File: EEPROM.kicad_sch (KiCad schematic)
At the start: 22 parts, among them IC1 PCA6408A_TSSOP, IC2 AT24CS01_SOT23, U2 TPS613221A_SOT-23-5

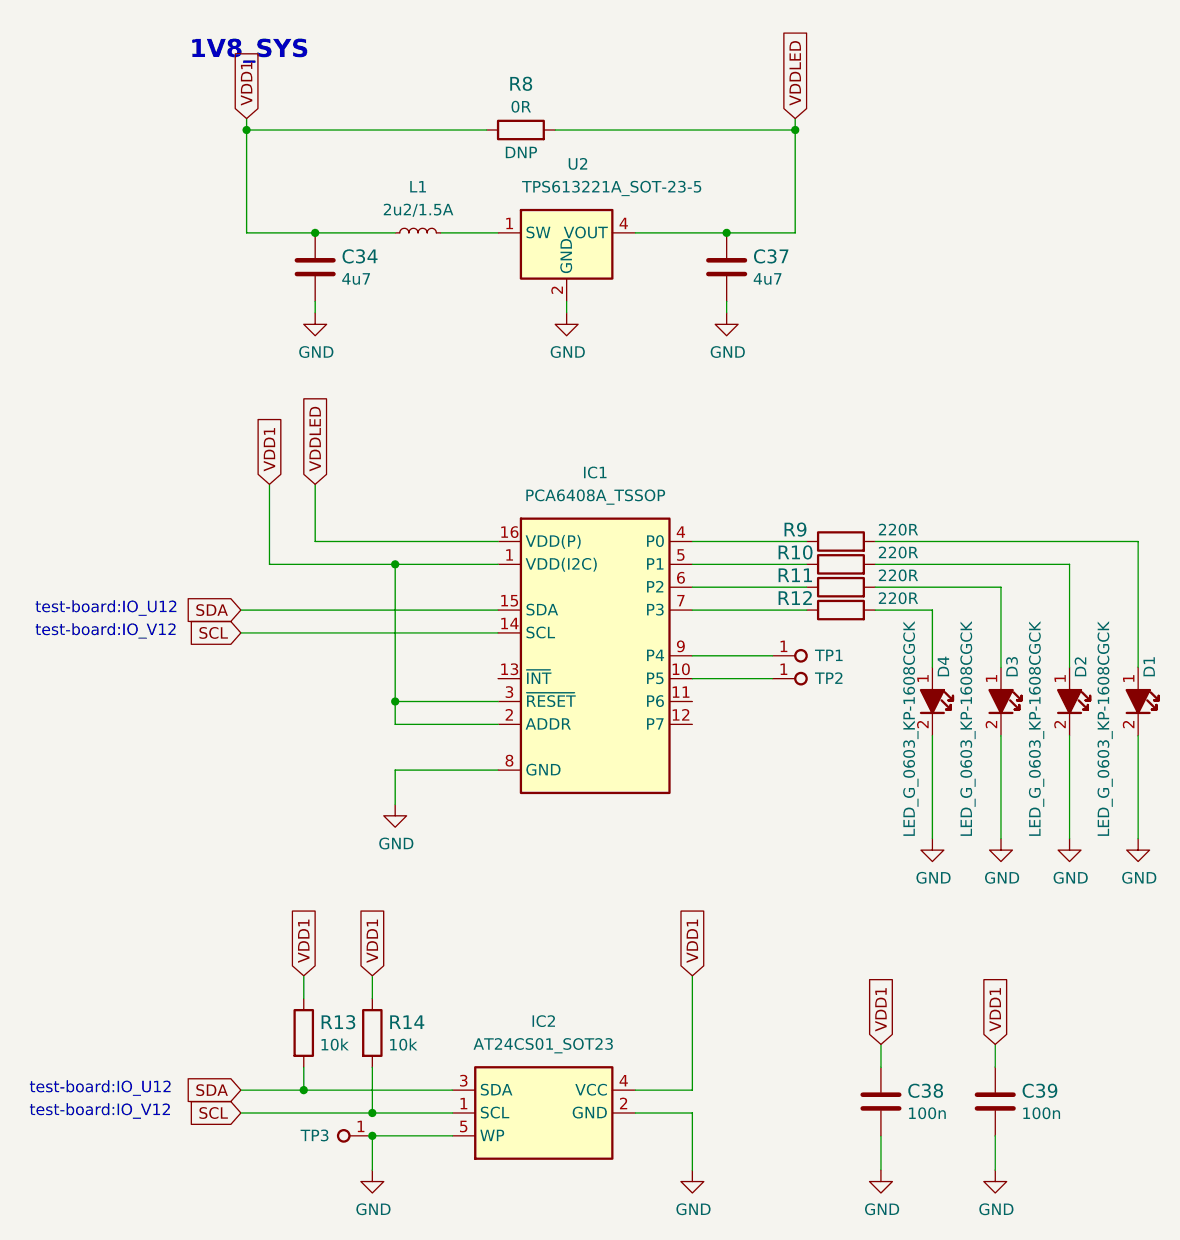
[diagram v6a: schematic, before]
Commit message: Introduce component standardization
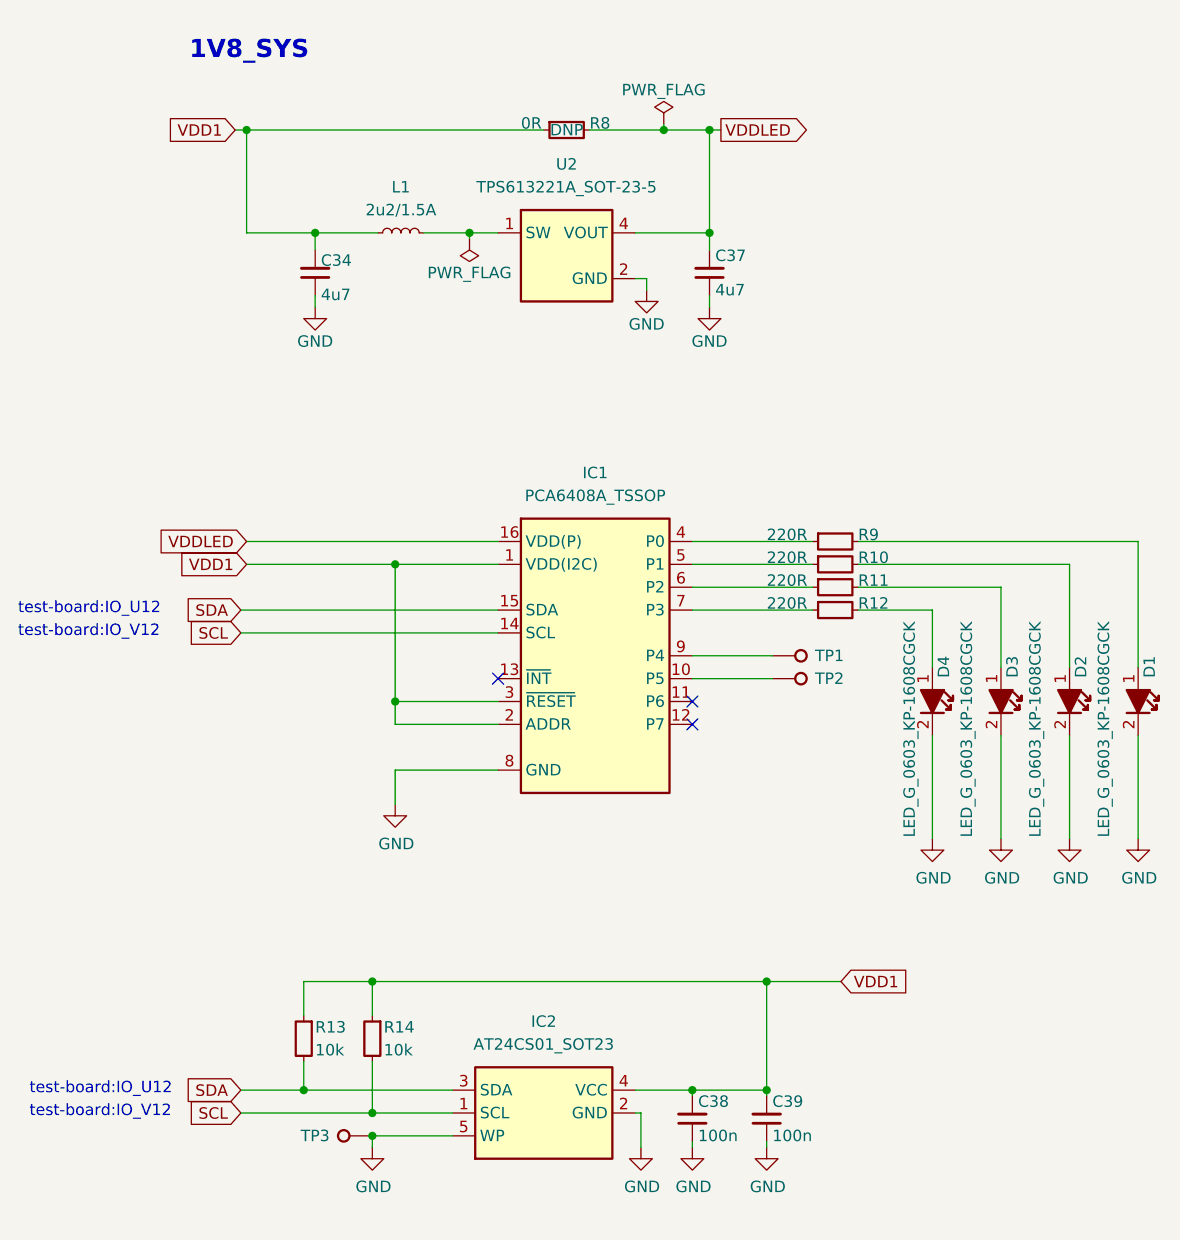
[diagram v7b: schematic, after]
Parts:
- C34, C37: footprint antmicro-footprints:C_0402_1005Metric -> lpddr4-testbed-footprints:C_0402_1005Metric; symbol antmicroCapacitors0402:C_4u7_0402 -> lpddr4-testbed:C_4u7_0402; Author (none) -> Antmicro; License (none) -> Apache-2.0; Manufacturer MURATA -> Murata
- C38, C39: footprint antmicro-footprints:C_0402_1005Metric -> lpddr4-testbed-footprints:C_0402_1005Metric; symbol antmicroCapacitors0402:C_100n_0402 -> lpddr4-testbed:C_100n_0402; Author (none) -> Antmicro; Dielectric (none) -> X5R; License (none) -> Apache-2.0; Voltage (none) -> 50V
- D1, D2, D3, D4: footprint antmicro-footprints:LED_0603_1608Metric_G -> lpddr4-testbed-footprints:LED_0603_1608Metric_G; symbol antmicroLEDIndicationDiscrete:LED_G_0603_KP-1608CGCK -> lpddr4-testbed:LED_G_0603_KP-1608CGCK
- IC1: footprint antmicro-footprints:TSSOP-16_4.4x5mm_P0.65mm -> lpddr4-testbed-footprints:TSSOP-16_4.4x5mm_P0.65mm; symbol antmicroInterfaceIOExpanders:PCA6408A_TSSOP -> lpddr4-testbed:PCA6408A_TSSOP
- IC2: footprint antmicro-footprints:SOT-23-5 -> lpddr4-testbed-footprints:SOT-23-5; symbol antmicroMemory:AT24CS01_SOT23 -> lpddr4-testbed:AT24CS01_SOT23
- L1: footprint antmicro-footprints:L_0806_2016Metric -> lpddr4-testbed-footprints:L_0806_2016Metric; symbol antmicroFixedInductors:L_2u2_1.5A_1285AS-H -> lpddr4-testbed:L_2u2_1.5A_1285AS-H
- R10, R11, R12, R9: footprint antmicro-footprints:R_0402_1005Metric -> lpddr4-testbed-footprints:R_0402_1005Metric; symbol antmicroResistors0402:R_220R_0402 -> lpddr4-testbed:R_220R_0402; Author (none) -> Antmicro; License (none) -> Apache-2.0; Tolerance (none) -> 1%
- R13, R14: footprint antmicro-footprints:R_0402_1005Metric -> lpddr4-testbed-footprints:R_0402_1005Metric; symbol antmicroResistors0402:R_10k_0402 -> lpddr4-testbed:R_10k_0402; Author (none) -> Antmicro; License (none) -> Apache-2.0; Tolerance (none) -> 1%
- R8: footprint antmicro-footprints:R_0402_1005Metric -> lpddr4-testbed-footprints:R_0402_1005Metric; symbol antmicroResistors0402:R_0R_0402 -> lpddr4-testbed:R_0R_0402; Author (none) -> Antmicro; Current (none) -> 1A; License (none) -> Apache-2.0; Manufacturer PANASONIC -> Panasonic
- TP1, TP2, TP3: footprint antmicro-footprints:TP_SMD_0.75mm -> lpddr4-testbed-footprints:TP_SMD_0.75mm; symbol antmicroTestPoints:TP_0.75mm_SMD -> lpddr4-testbed:TP_0.75mm_SMD
- U2: footprint antmicro-footprints:SOT-23-5 -> lpddr4-testbed-footprints:SOT-23-5; symbol antmicroDCDCConverters:TPS613221A_SOT-23-5 -> lpddr4-testbed:TPS613221A_SOT-23-5
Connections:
- net GND: now also C34.1, C37.1, C38.1, C39.1; no longer C34.2, C37.2, C38.2, C39.2
- net VDD1: now also C34.2, C38.2, C39.2; no longer C34.1, C38.1, C39.1
- net VDDLED: now also C37.2; no longer C37.1
- net at U2.3 (NC): no longer U2.5 (NC)
- no-connect marks 0 -> 3
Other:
- title: (none) -> LPDDR4 testbed
- moved on the sheet: C34, C37, C38, C39, L1, R10, R11, R12, R13, R14, R8, R9

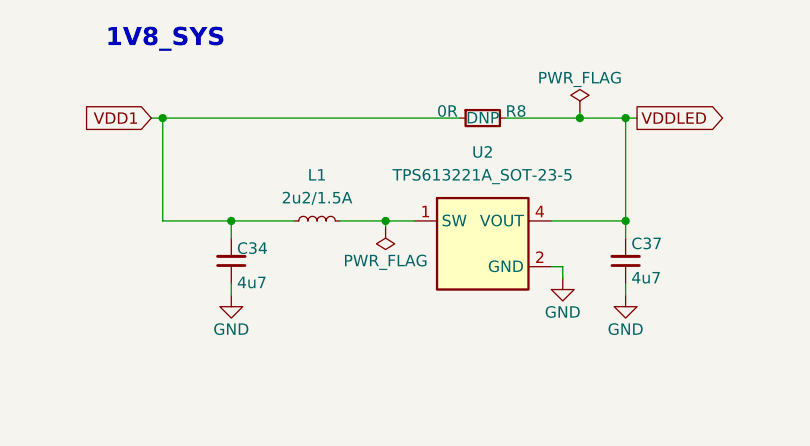
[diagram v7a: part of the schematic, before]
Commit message: [#56947] Correct component references
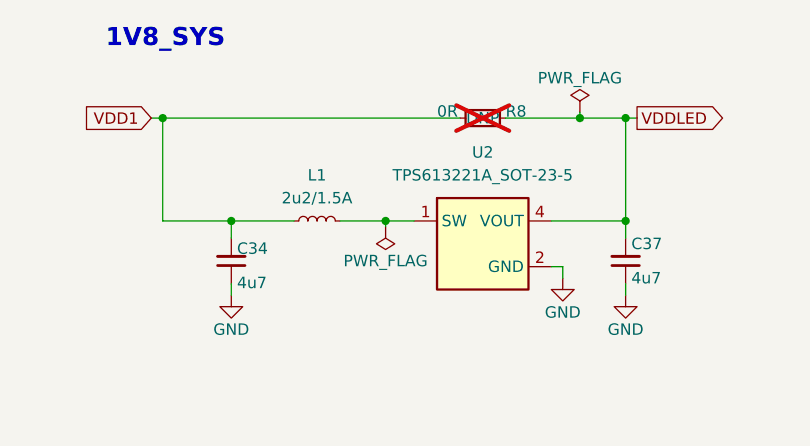
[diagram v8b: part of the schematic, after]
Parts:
- C34, C37: footprint lpddr4-testbed-footprints:C_0402_1005Metric -> antmicro-footprints:C_0402_1005Metric; symbol lpddr4-testbed:C_4u7_0402 -> antmicroCapacitors0402:C_4u7_0402
- C38, C39: footprint lpddr4-testbed-footprints:C_0402_1005Metric -> antmicro-footprints:C_0402_1005Metric; symbol lpddr4-testbed:C_100n_0402 -> antmicroCapacitors0402:C_100n_0402
- D1, D2, D3, D4: footprint lpddr4-testbed-footprints:LED_0603_1608Metric_G -> antmicro-footprints:LED_0603_1608Metric_G; symbol lpddr4-testbed:LED_G_0603_KP-1608CGCK -> antmicroLEDIndicationDiscrete:LED_G_0603_KP-1608CGCK
- IC1: footprint lpddr4-testbed-footprints:TSSOP-16_4.4x5mm_P0.65mm -> antmicro-footprints:TSSOP-16_4.4x5mm_P0.65mm; symbol lpddr4-testbed:PCA6408A_TSSOP -> antmicroInterfaceIOExpanders:PCA6408A_TSSOP
- IC2: footprint lpddr4-testbed-footprints:SOT-23-5 -> antmicro-footprints:SOT-23-5; symbol lpddr4-testbed:AT24CS01_SOT23 -> antmicroMemory:AT24CS01_SOT23
- L1: symbol lpddr4-testbed:L_2u2_1.5A_1285AS-H -> antmicroFixedInductors:L_2u2_1.5A_0806
- R10, R11, R12, R9: footprint lpddr4-testbed-footprints:R_0402_1005Metric -> antmicro-footprints:R_0402_1005Metric; symbol lpddr4-testbed:R_220R_0402 -> antmicroResistors0402:R_220R_0402
- R13, R14: footprint lpddr4-testbed-footprints:R_0402_1005Metric -> antmicro-footprints:R_0402_1005Metric; symbol lpddr4-testbed:R_10k_0402 -> antmicroResistors0402:R_10k_0402
- R8: footprint lpddr4-testbed-footprints:R_0402_1005Metric -> antmicro-footprints:R_0402_1005Metric; symbol lpddr4-testbed:R_0R_0402 -> antmicroResistors0402:R_0R_0402; now not fitted; now left out of the parts list
- TP1, TP2, TP3: footprint lpddr4-testbed-footprints:TP_SMD_0.75mm -> antmicro-footprints:TP_SMD_0.75mm; symbol lpddr4-testbed:TP_0.75mm_SMD -> antmicroTestPoints:TP_0.75mm_SMD
- U2: footprint lpddr4-testbed-footprints:SOT-23-5 -> antmicro-footprints:SOT-23-5; symbol lpddr4-testbed:TPS613221A_SOT-23-5 -> antmicroDCDCConverters:TPS613221A_SOT-23-5
